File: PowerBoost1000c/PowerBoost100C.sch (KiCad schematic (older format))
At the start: 26 parts, among them J4 CONN_01X08, U2 MCP73871, U4 TPS61090RSAR

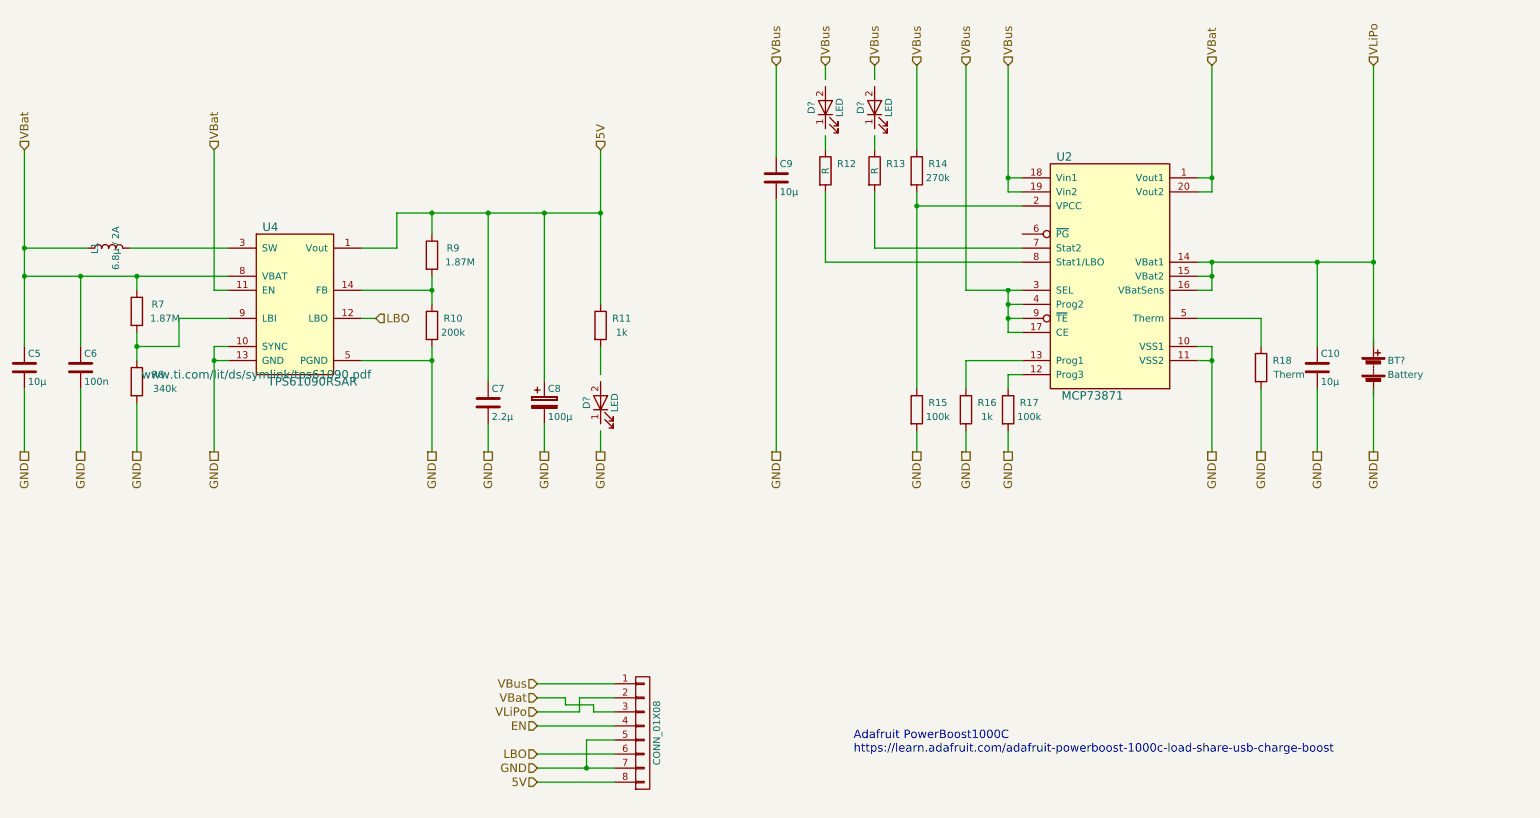
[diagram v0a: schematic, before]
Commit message: modified PowerBoost
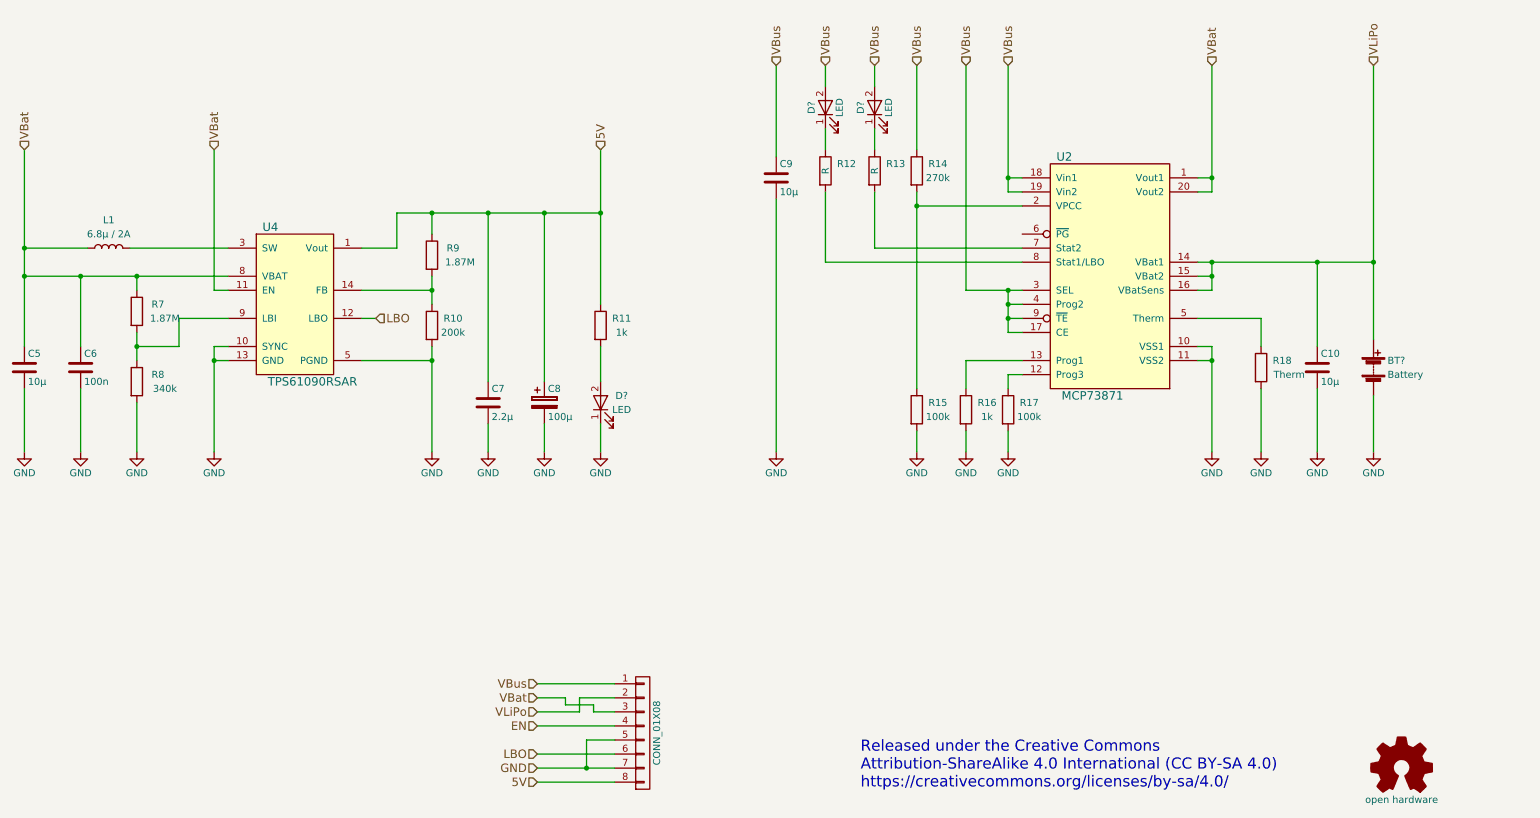
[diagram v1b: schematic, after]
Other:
- note added: "Released under the Creative Commons\nAttribution-ShareAlike 4.0 International (CC BY-SA 4.0) \nhttps://creativecommons.org/licenses/by-sa/4.0/"
- note removed: "Adafruit PowerBoost1000C\nhttps://learn.adafruit.com/adafruit-powerboost-1000c-load-share-usb-charge-boost"

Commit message: used MCP73871 of lib instead of self drawn one
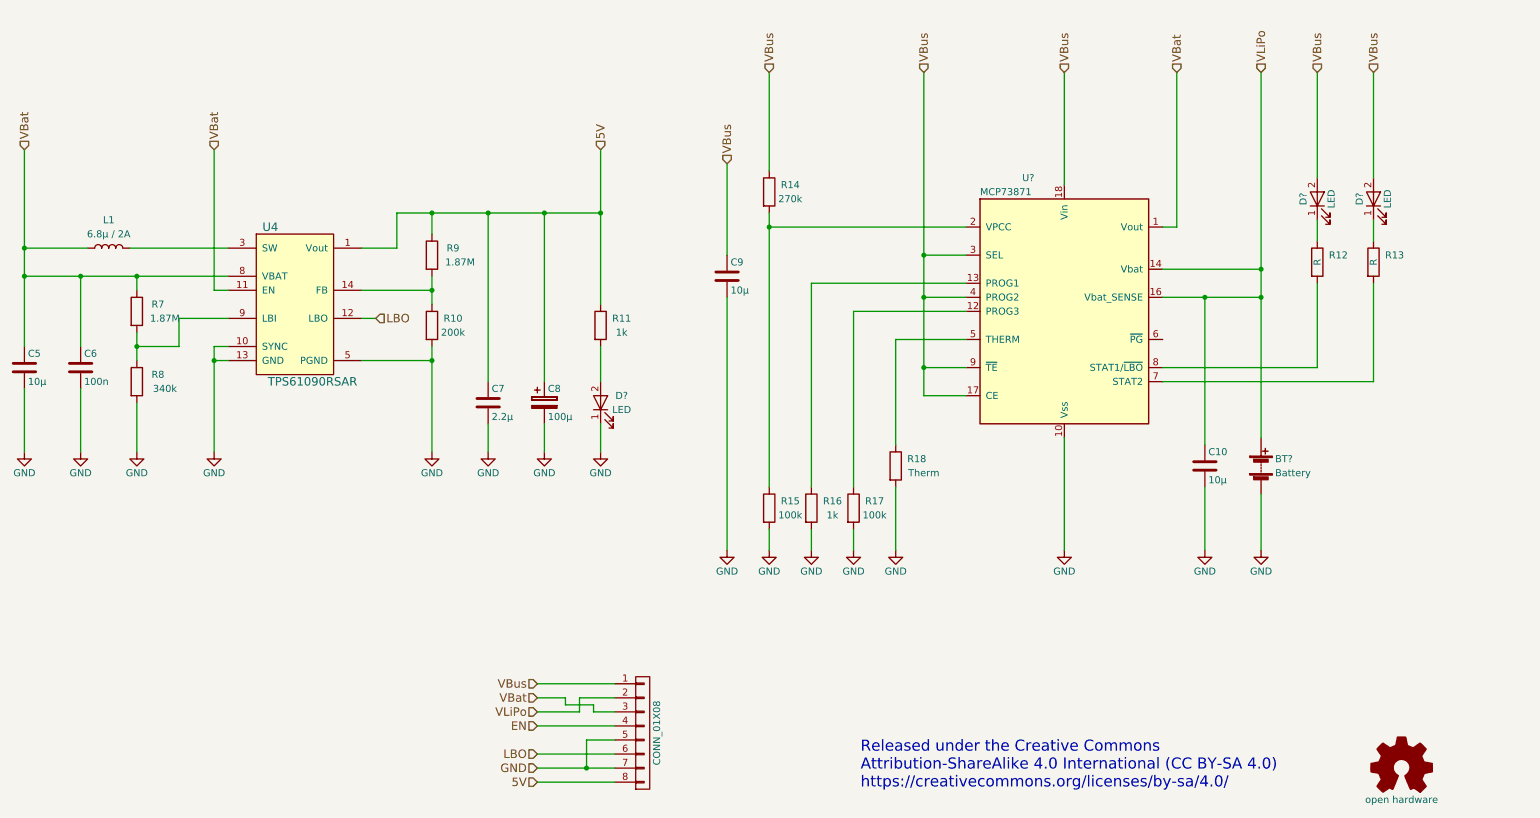
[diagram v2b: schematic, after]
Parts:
- removed U2: MCP73871, symbol MCP37871
- added U?: MCP73871, Housings_DFN_QFN:QFN-20-1EP_4x4mm_Pitch0.5mm, symbol MCP73871
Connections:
- net GND: now also U?.10 (Vss), U?.11 (Vss), U?.21 (Vss)
- net VBat: now also U?.1 (Vout), U?.20 (Vout)
- net VBus: now also U?.17 (CE), U?.18 (Vin), U?.19 (Vin), U?.3 (SEL), U?.4 (PROG2), U?.9 (~TE)
- net VLiPo: now also U?.14 (Vbat), U?.15 (Vbat), U?.16 (Vbat_SENSE)
- net at R18.1: now also U?.5 (THERM)
- net at R17.1: now also U?.12 (PROG3)
- net at R16.1: now also U?.13 (PROG1)
- net at R14.2, R15.1: now also U?.2 (VPCC)
- net at R13.2: now also U?.7 (STAT2)
- net at R12.2: now also U?.8 (STAT1/~LBO~)
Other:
- moved on the sheet: BT?, C10, C9, D?, R12, R13, R14, R15, R16, R17, R18
